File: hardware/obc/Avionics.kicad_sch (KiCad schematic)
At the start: 41 parts, among them J305 Conn_01x05, U101 MAX706RESA, U103 RP2350_80QFN, Y101 Crystal_GND24_Small

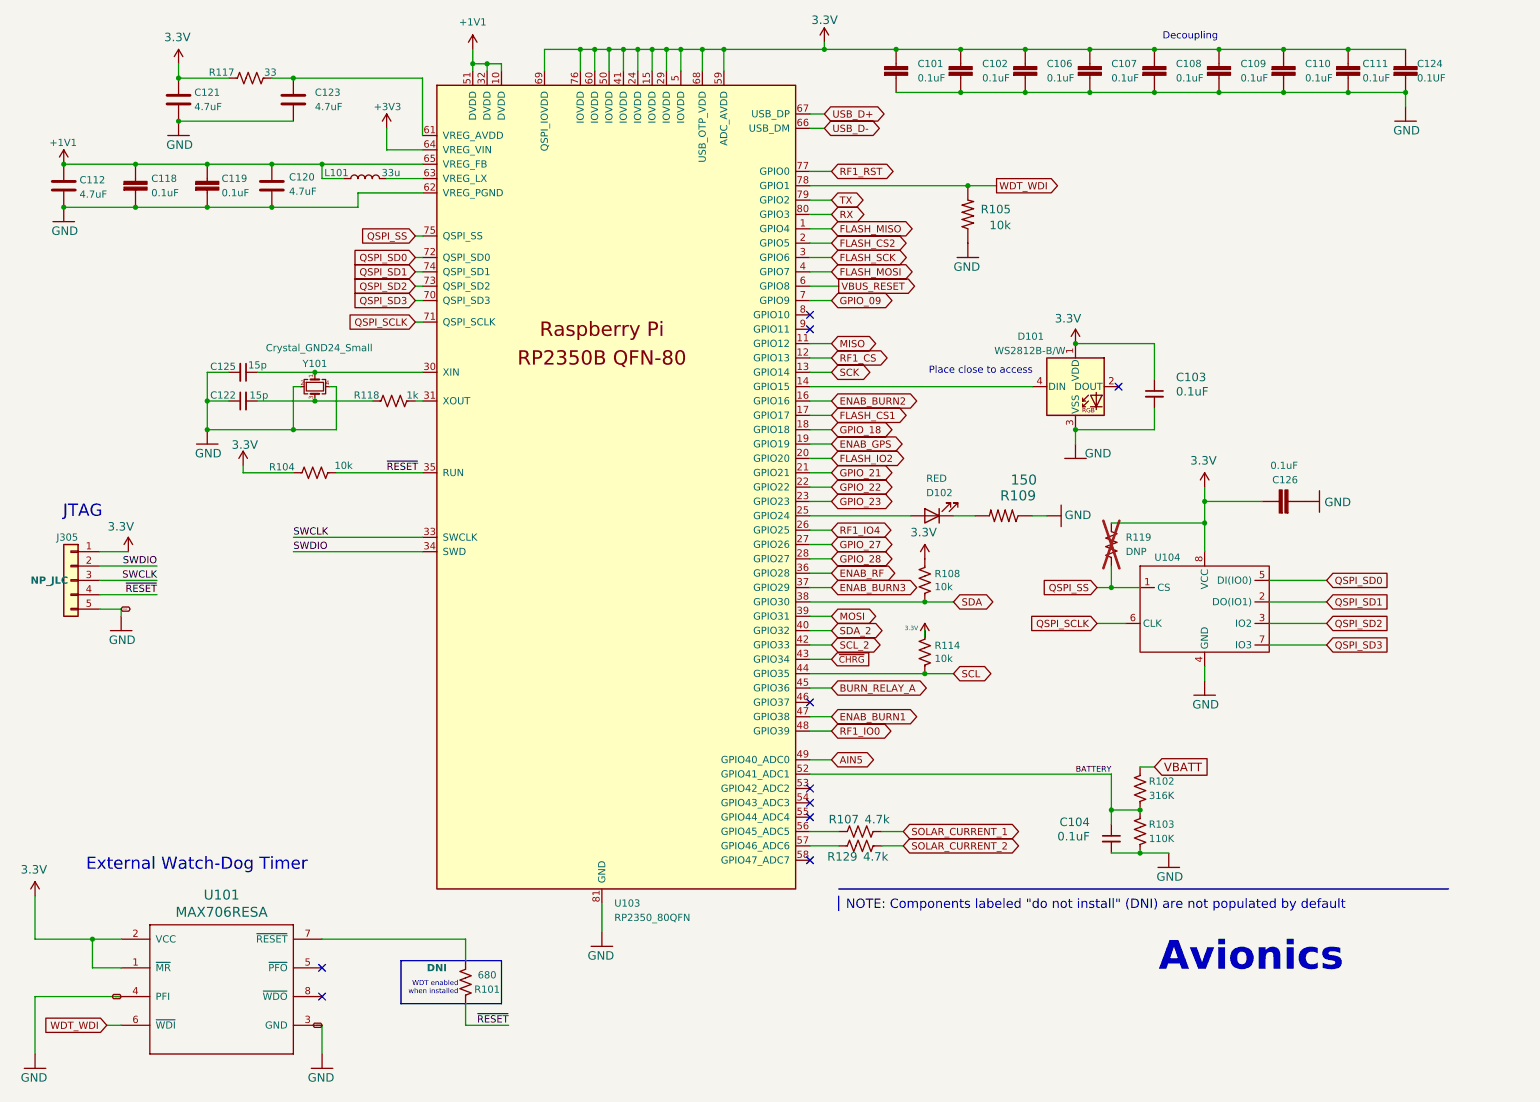
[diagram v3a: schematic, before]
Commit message: OBC: Added new power supervisor and watch dog circuit
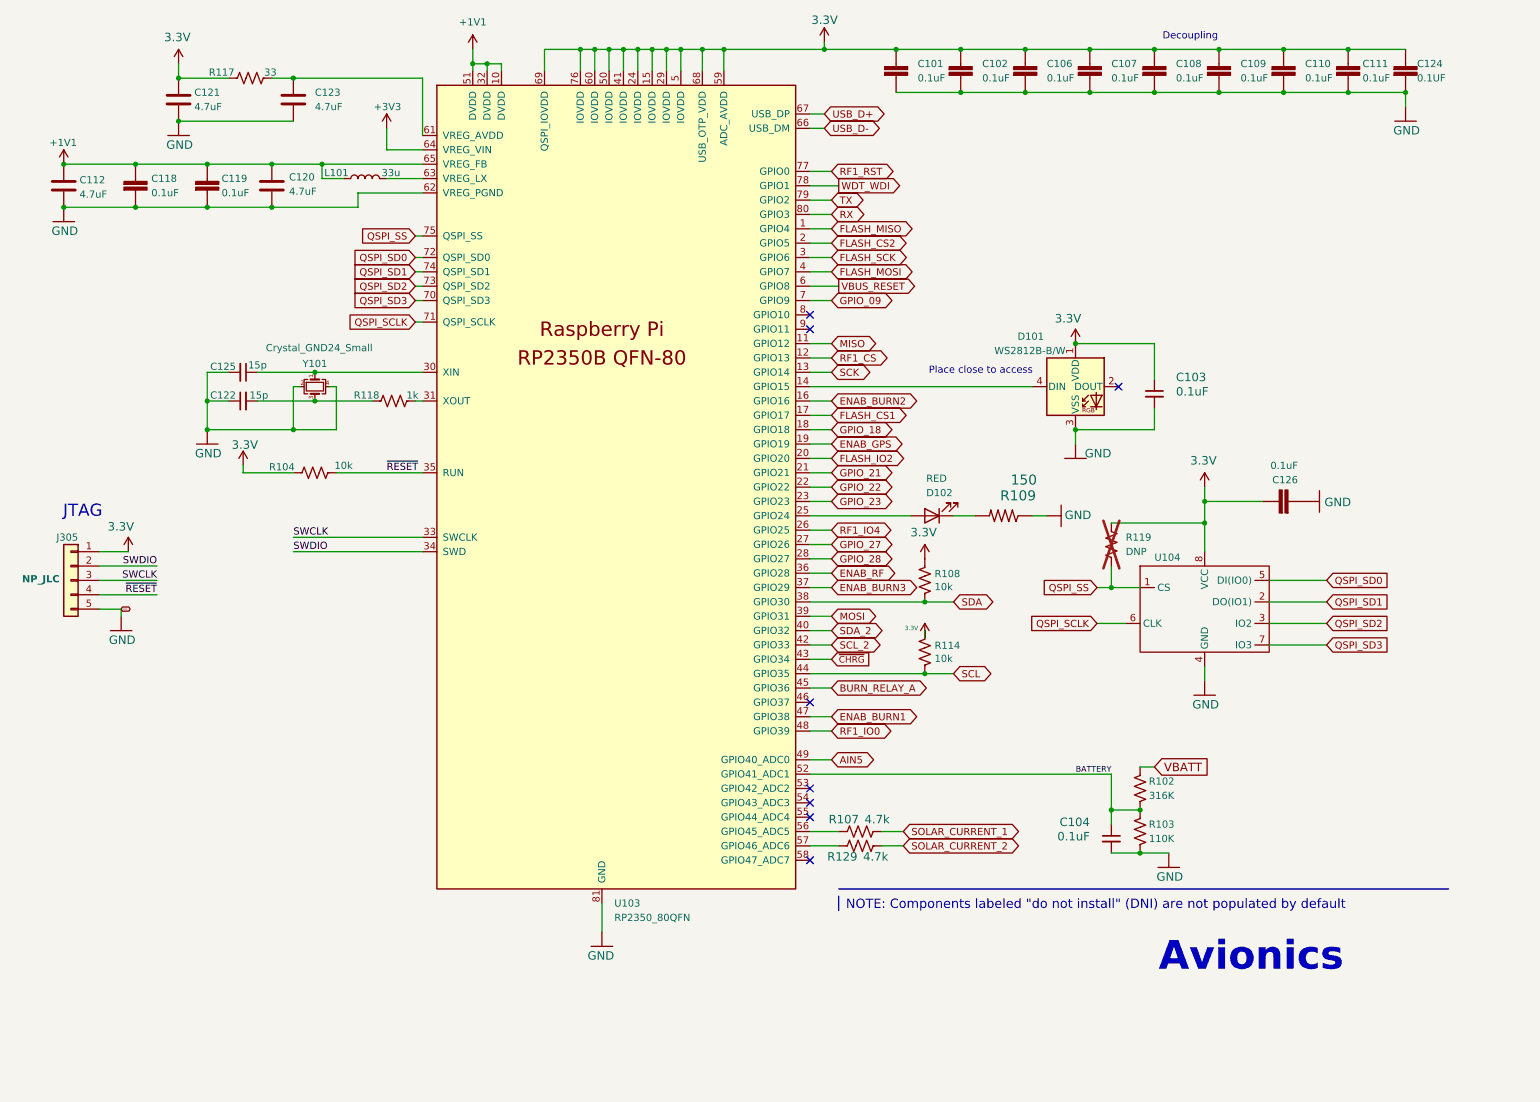
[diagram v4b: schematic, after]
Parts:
- removed R101: 680, Resistor_SMD:R_0603_1608Metric, symbol Device:R_US
- removed R105: 10k, Resistor_SMD:R_0603_1608Metric, symbol mainboard:R-US_R0603
- removed U101: MAX706RESA, Package_SO:SO-8_3.9x4.9mm_P1.27mm, symbol mainboard:MAX708RESA-T
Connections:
- no-connect marks 10 -> 8
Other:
- note removed: "External Watch-Dog Timer"
- note removed: "WDT enabled when installed"

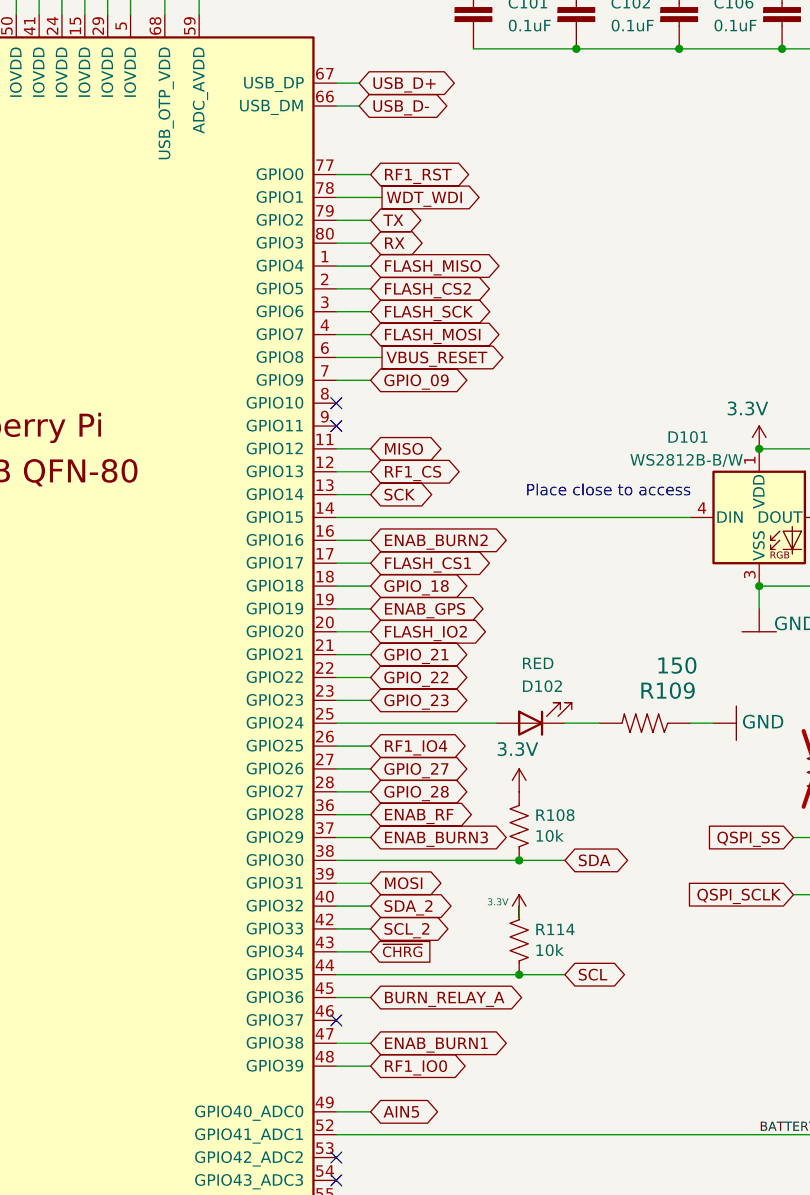
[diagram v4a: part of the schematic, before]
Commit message: OBC: Freed up GPIO0 and added footprints
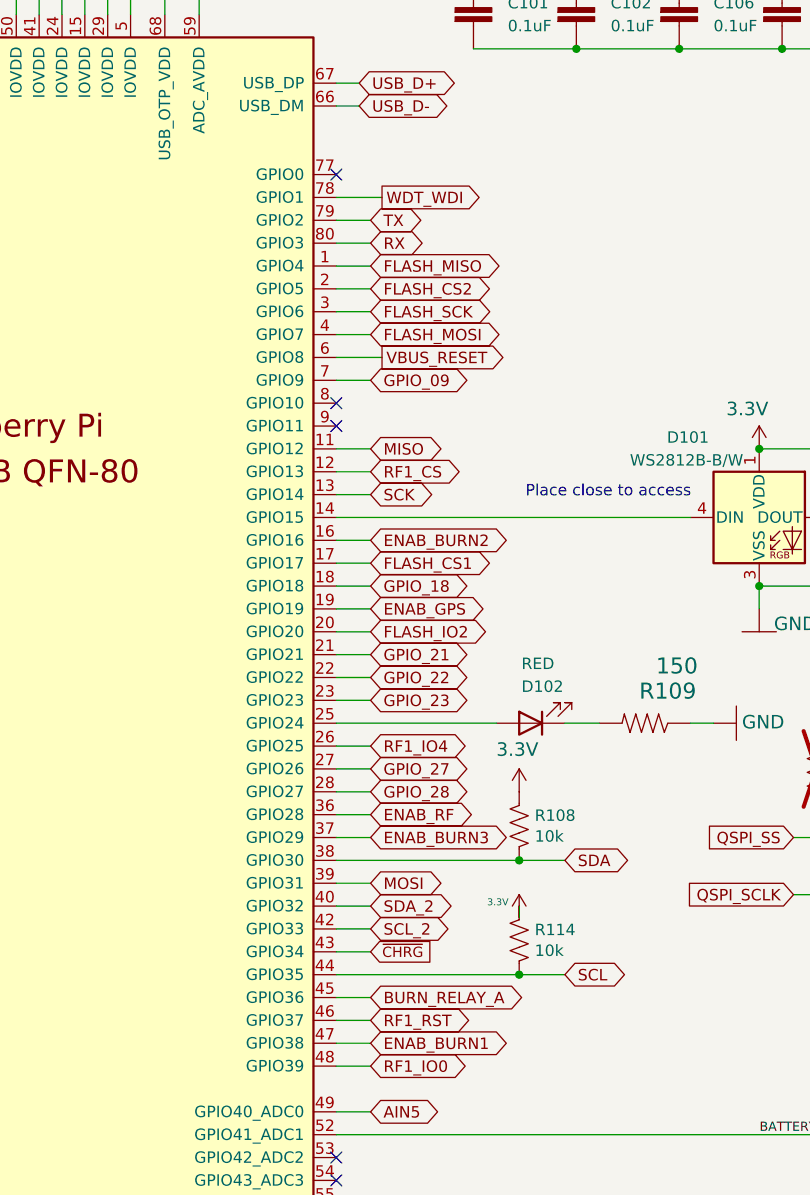
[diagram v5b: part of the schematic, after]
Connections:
- net RF1_RST: now also U103.46 (GPIO37); no longer U103.77 (GPIO0)
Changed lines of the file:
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@@
-	)
-	(no_connect
-		(at 153.67 134.62)
 	)
 	(no_connect
@@
 	)
 	(no_connect
+		(at 153.67 40.64)
+	)
+	(no_connect
 		(at 153.67 68.58)
 	)
@@
 	(wire
 		(pts
+			(xy 153.67 134.62) (xy 157.48 134.62)
+		)
+		(stroke
+			(width 0)
+			(type default)
+		)
+	)
+	(wire
+		(pts
 			(xy 66.04 76.2) (xy 85.09 76.2)
 		)
@@
 		(pts
 			(xy 153.67 48.26) (xy 157.48 48.26)
-		)
-		(stroke
-			(width 0)
-			(type default)
-		)
-	)
-	(wire
-		(pts
-			(xy 153.67 40.64) (xy 157.48 40.64)
 		)
 		(stroke
@@
 		)
 	)
+	(global_label "RF1_RST"
+		(shape bidirectional)
+		(at 157.48 134.62 0)
+		(effects
+			(font
+				(size 1.27 1.27)
+			)
+			(justify left)
+		)
+		(property "Intersheetrefs" "${INTERSHEET_REFS}"
+			(at 157.48 134.62 0)
+			(effects
+				(font
+					(size 1.27 1.27)
+				)
+				(hide yes)
+			)
+		)
+	)
 	(global_label "SCL"
 		(shape bidirectional)
@@
 				(hide yes)
 			)
-		)
-	)
-	(global_label "RF1_RST"
-		(shape bidirectional)
-		(at 157.48 40.64 0)
-		(effects
-			(font
-				(size 1.27 1.27)
-			)
-			(justify left)
-		)
-		(property "Intersheetrefs" "${INTERSHEET_REFS}"
-			(at 157.48 40.64 0)
-			(effects
-				(font
-					(size 1.27 1.27)
-				)
-				(hide yes)
-			)

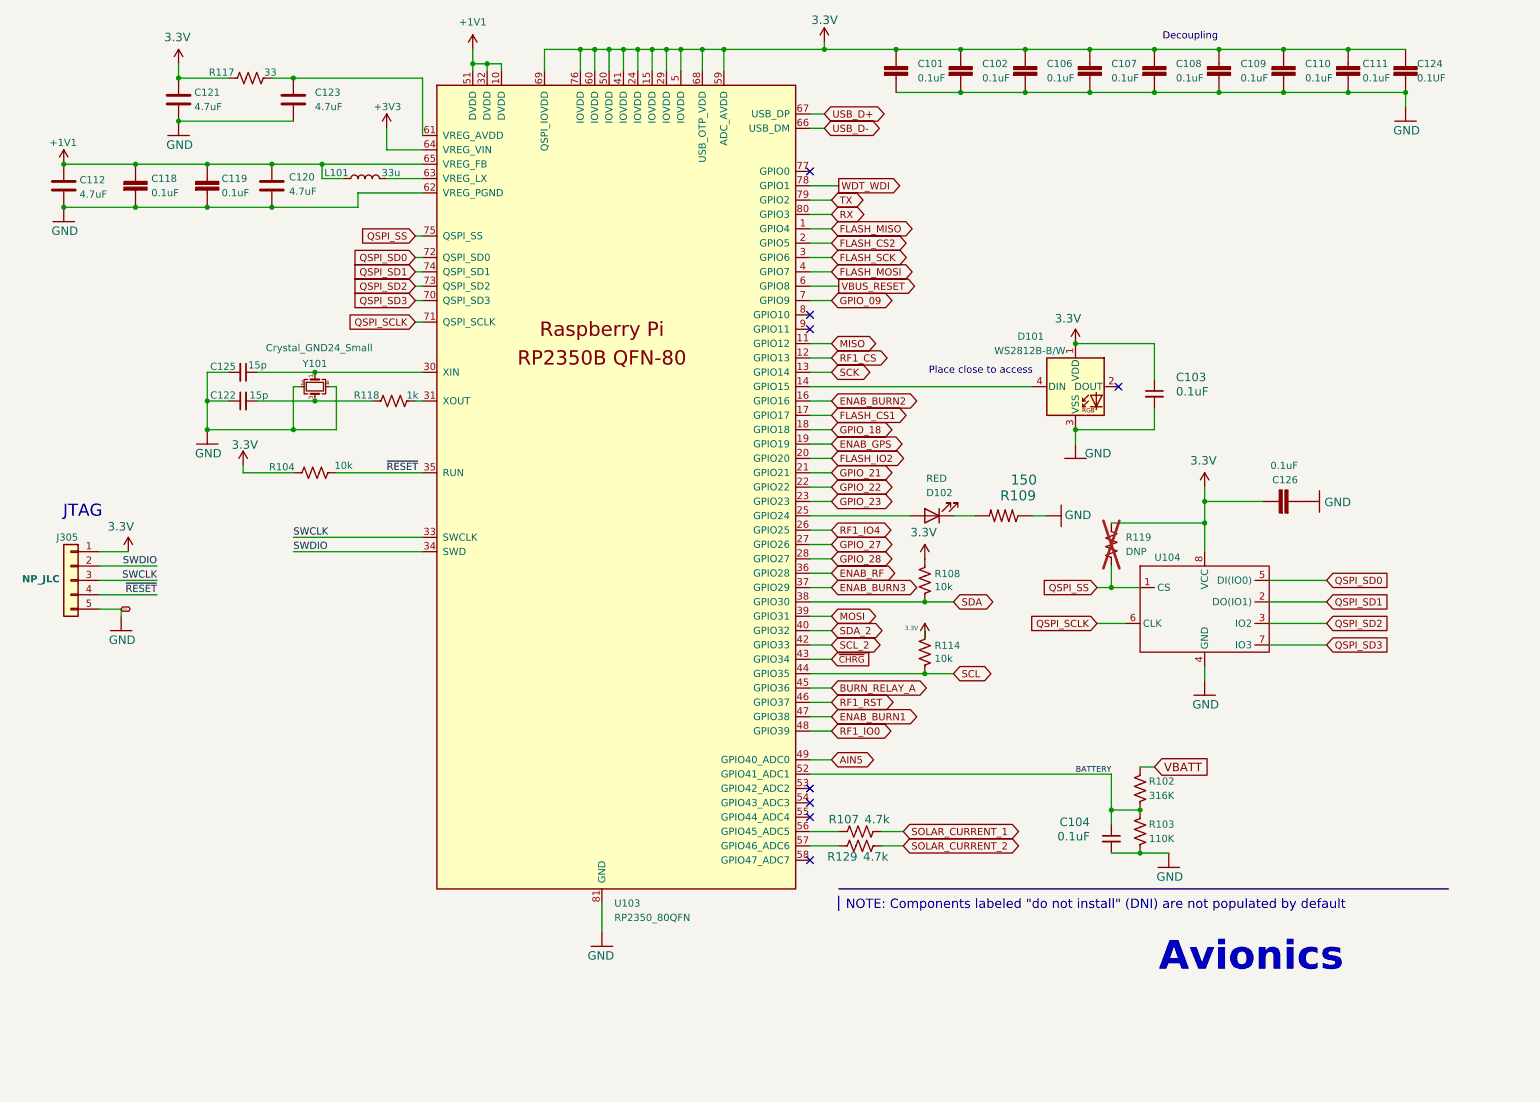
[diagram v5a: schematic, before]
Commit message: obc: changed flash memory to PSRAM
- Fixed MRAM symbol
- Removed Flash memory for new PSRAM
- Changed labels on Avionics page to match format
- Added another 0.1uF capacitor to VRAG pins
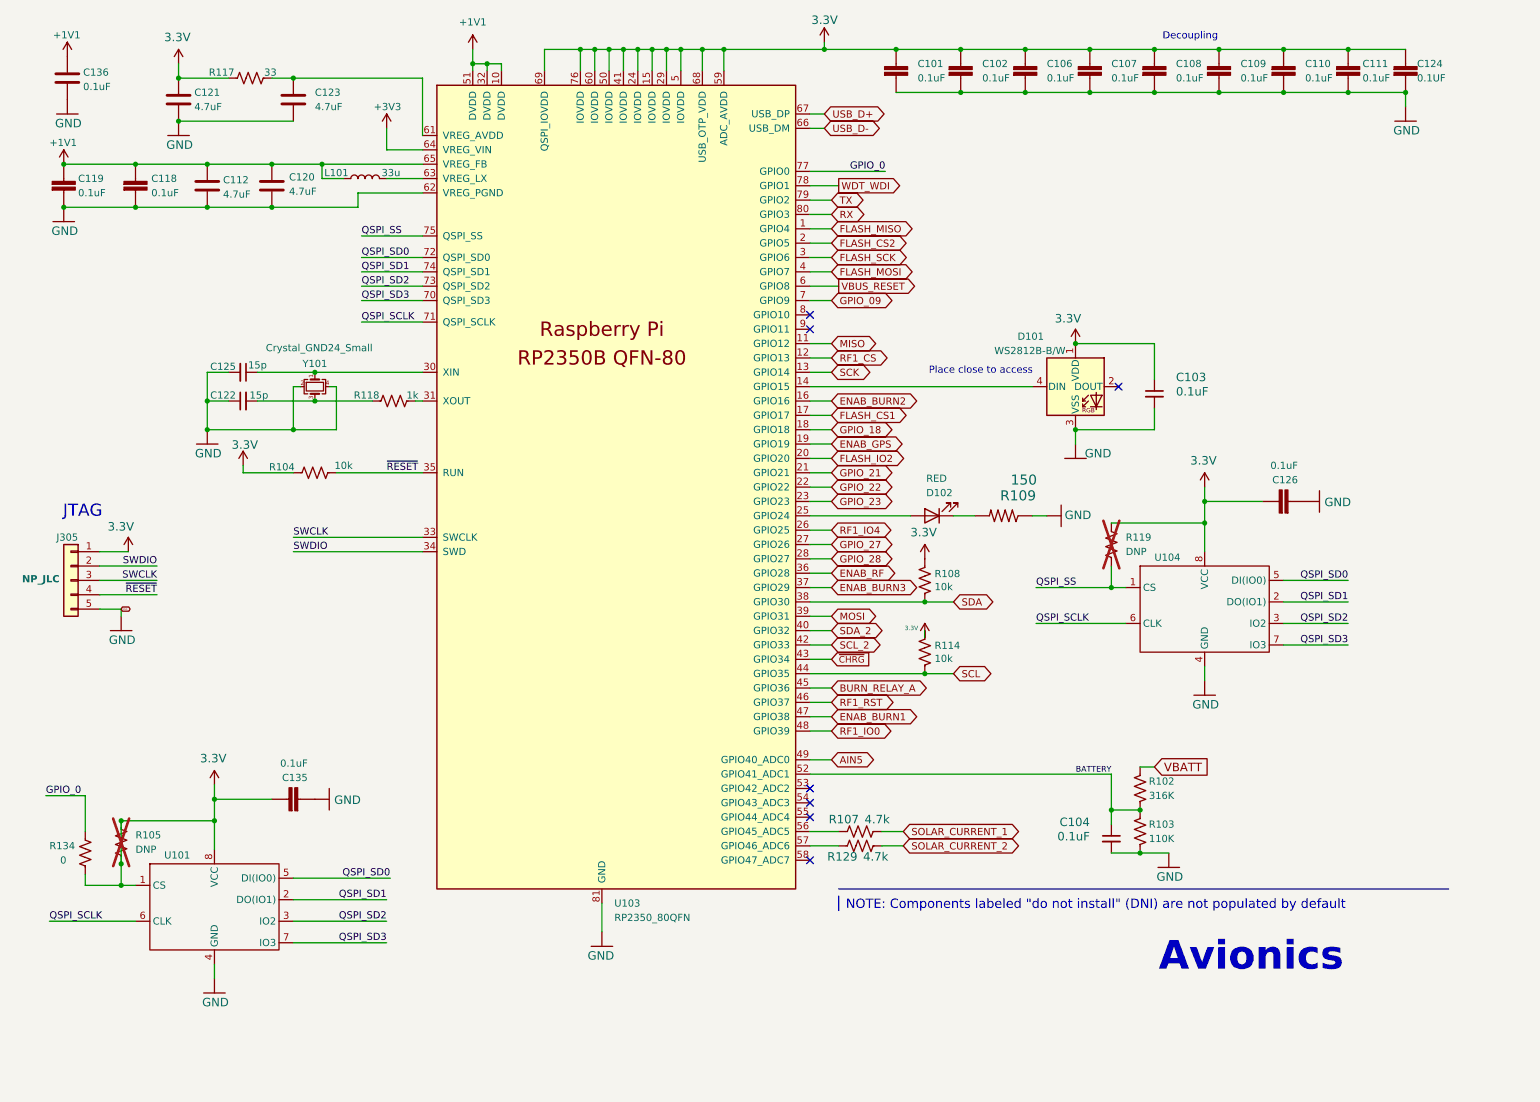
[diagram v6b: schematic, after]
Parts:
- added C135: 0.1uF, Capacitor_SMD:C_0603_1608Metric, symbol mainboard:0.1UF-0603-25V-5%
- added C136: 0.1uF, Capacitor_SMD:C_0603_1608Metric, symbol Device:C
- added R105: DNP, Resistor_SMD:R_0603_1608Metric, symbol Device:R_US
- added R134: 0, symbol Device:R_US
- added U101: ~, Package_SON:WSON-8-1EP_6x5mm_P1.27mm_EP3.4x4mm, symbol mram_wson:MRAM_WSON
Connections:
- net +1V1: now also C136.1
- net 3.3V: now also C135.1, R105.1, R105.2, R134.2, U101.1 (CS), U101.8 (VCC)
- net GND: now also C135.2, C136.2, U101.4 (GND)
- net QSPI_SCLK: now also U101.6 (CLK)
- net QSPI_SD0: now also U101.5 (DI(IO0))
- net QSPI_SD1: now also U101.2 (DO(IO1))
- net QSPI_SD2: now also U101.3 (IO2)
- net QSPI_SD3: now also U101.7 (IO3)
- net GPIO_0: now reaches U103.77 (GPIO0)
- net GPIO_0: now also R134.1
- no-connect marks 8 -> 7
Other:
- moved on the sheet: C112, C119, U104
